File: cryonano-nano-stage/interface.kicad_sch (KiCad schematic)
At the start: 0 parts

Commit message: sch improved
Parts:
- added C29, C32, C33, C34: 1u, Capacitor_SMD:C_0603_1608Metric, symbol Device:C_Small
- added C67: 100n, Capacitor_SMD:C_0603_1608Metric, symbol Device:C_Small
- added C68: 10u, Capacitor_SMD:C_0805_2012Metric, symbol Device:C_Small
- added R41, R42, R43, R44, R51, R53, R55, R56: 10k, Resistor_SMD:R_0603_1608Metric, symbol Device:R_Small
- added R45, R46, R47, R48, R49, R50, R52, R54: 0R, Resistor_SMD:R_0603_1608Metric, symbol Device:R_Small
- added U7, U8: LP5907MFX-3.3_NOPB, SOT95P280X145-5N, symbol symbols:LP5907MFX-3.3_NOPB
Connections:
- new net: R55.2, R56.1
- new net: R49.2, R51.1, R53.2, R55.1
- new net: R41.1, R45.2
- new net: R41.2, R42.1, R44.1, R48.2
- new net: R52.2, R53.1
- new net: R43.1, R44.2
- new net +3V3_1: C32.1, R45.1, U7.5 (OUT)
- new net +3V3_2: C34.1, R52.1, U8.5 (OUT)
- new net +5V0IN: C29.1, C33.1, C67.1, C68.1, U7.1 (IN), U7.3 (EN), U8.1 (IN), U8.3 (EN)
- new net 0V0IN: C29.2, C32.2, C33.2, C34.2, C67.2, C68.2, R46.2, R54.2, U7.2 (GND), U8.2 (GND)
- new net RTD1_A: R42.2
- new net RTD1_B: R43.2, R46.1, R47.2
- new net RTD1_REF+: R48.1
- new net RTD1_REF-: R47.1
- new net RTD2_A: R51.2
- new net RTD2_B: R50.2, R54.1, R56.2
- new net RTD2_REF+: R49.1
- new net RTD2_REF-: R50.1
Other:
- note added: "Power conditioning."
- company: (none) -> Cryonano Labs Pvt. Ltd.
- title: (none) -> Nano stage controller

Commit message: sch improved
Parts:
- C67: now not fitted
- C68: value 10u -> 100n; footprint Capacitor_SMD:C_0805_2012Metric -> Capacitor_SMD:C_0603_1608Metric; Tolerence (none) -> 10%; now not fitted
- R41, R42, R43, R44, R45, R46, R47, R48, R49, R50, R51, R52, R53, R54, R55, R56: footprint Resistor_SMD:R_0603_1608Metric -> Resistor_SMD:R_0805_2012Metric
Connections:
- net EQ2-: now reaches R55.2, R56.1
- net EQ1-: now reaches R43.1, R44.2
- net RTD1_A renamed EQ1+
- net RTD2_A renamed EQ2+

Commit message: sch improved
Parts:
- removed C29, C32, C33, C34: 1u, Capacitor_SMD:C_0603_1608Metric, symbol Device:C_Small
- removed C67, C68: 100n, Capacitor_SMD:C_0603_1608Metric, symbol Device:C_Small
- removed U7, U8: LP5907MFX-3.3_NOPB, SOT95P280X145-5N, symbol symbols:LP5907MFX-3.3_NOPB
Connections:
- net +3V3_2 is gone; now on net EXCITATION: R52.1
- net +3V3_1 renamed EXCITATION
- net 0V0IN renamed REF0
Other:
- note removed: "Power conditioning."
- moved on the sheet: R41, R42, R43, R44, R45, R46, R47, R48, R49, R50, R51, R52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

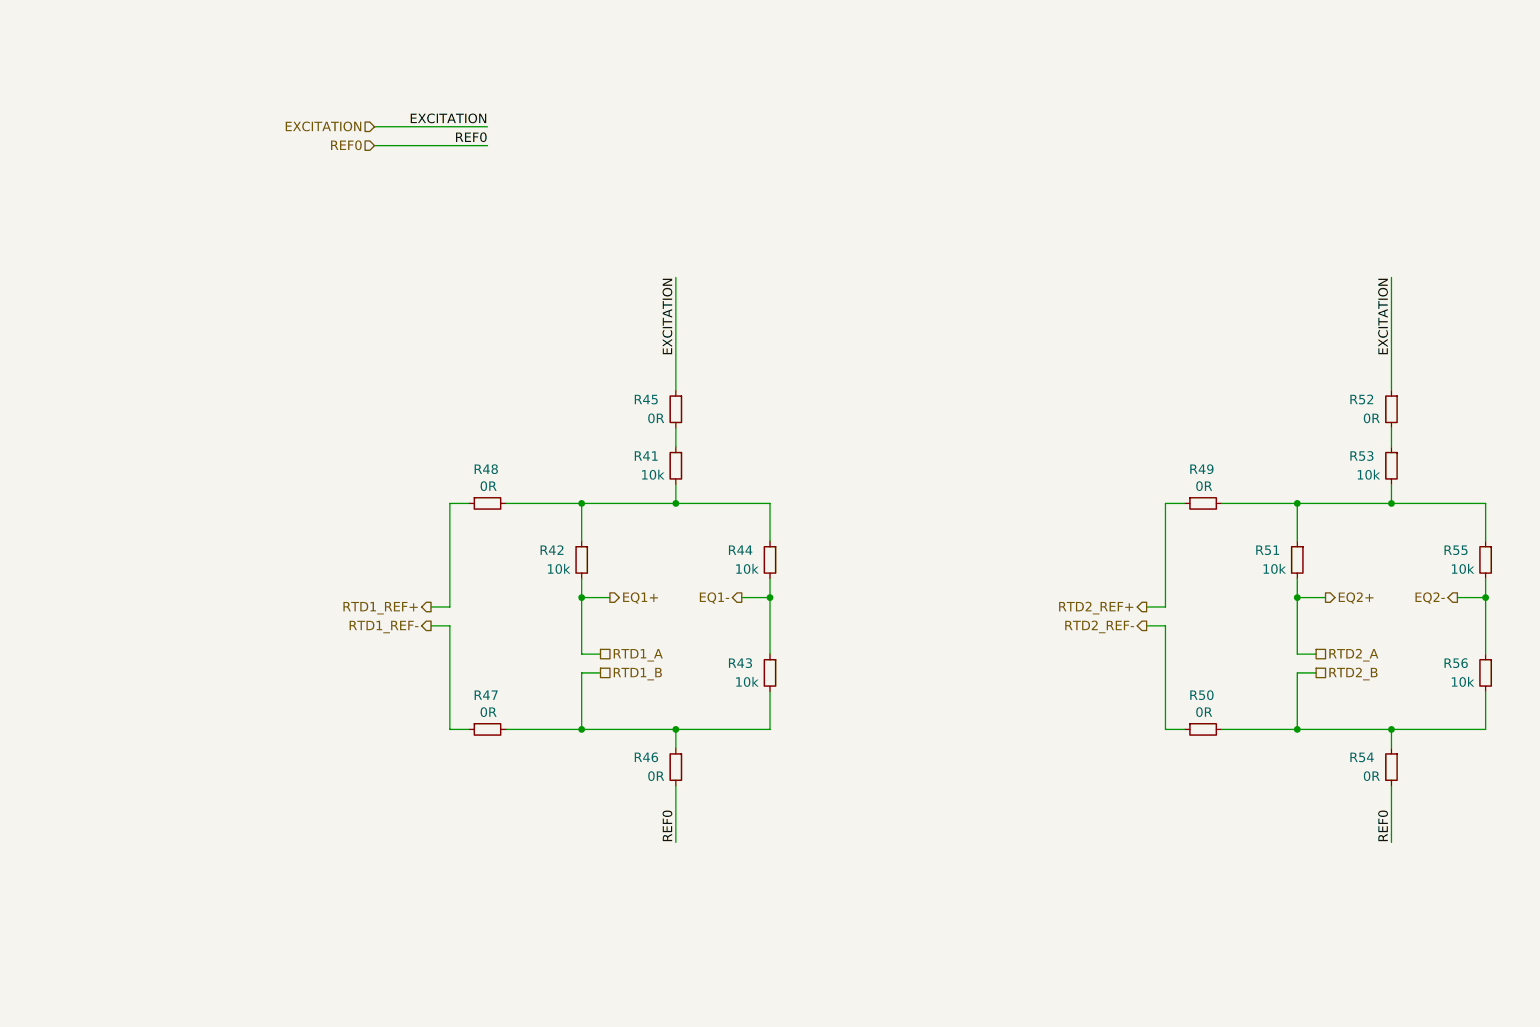
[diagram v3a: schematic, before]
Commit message: pcb drc ok. 68 ohm matching pending
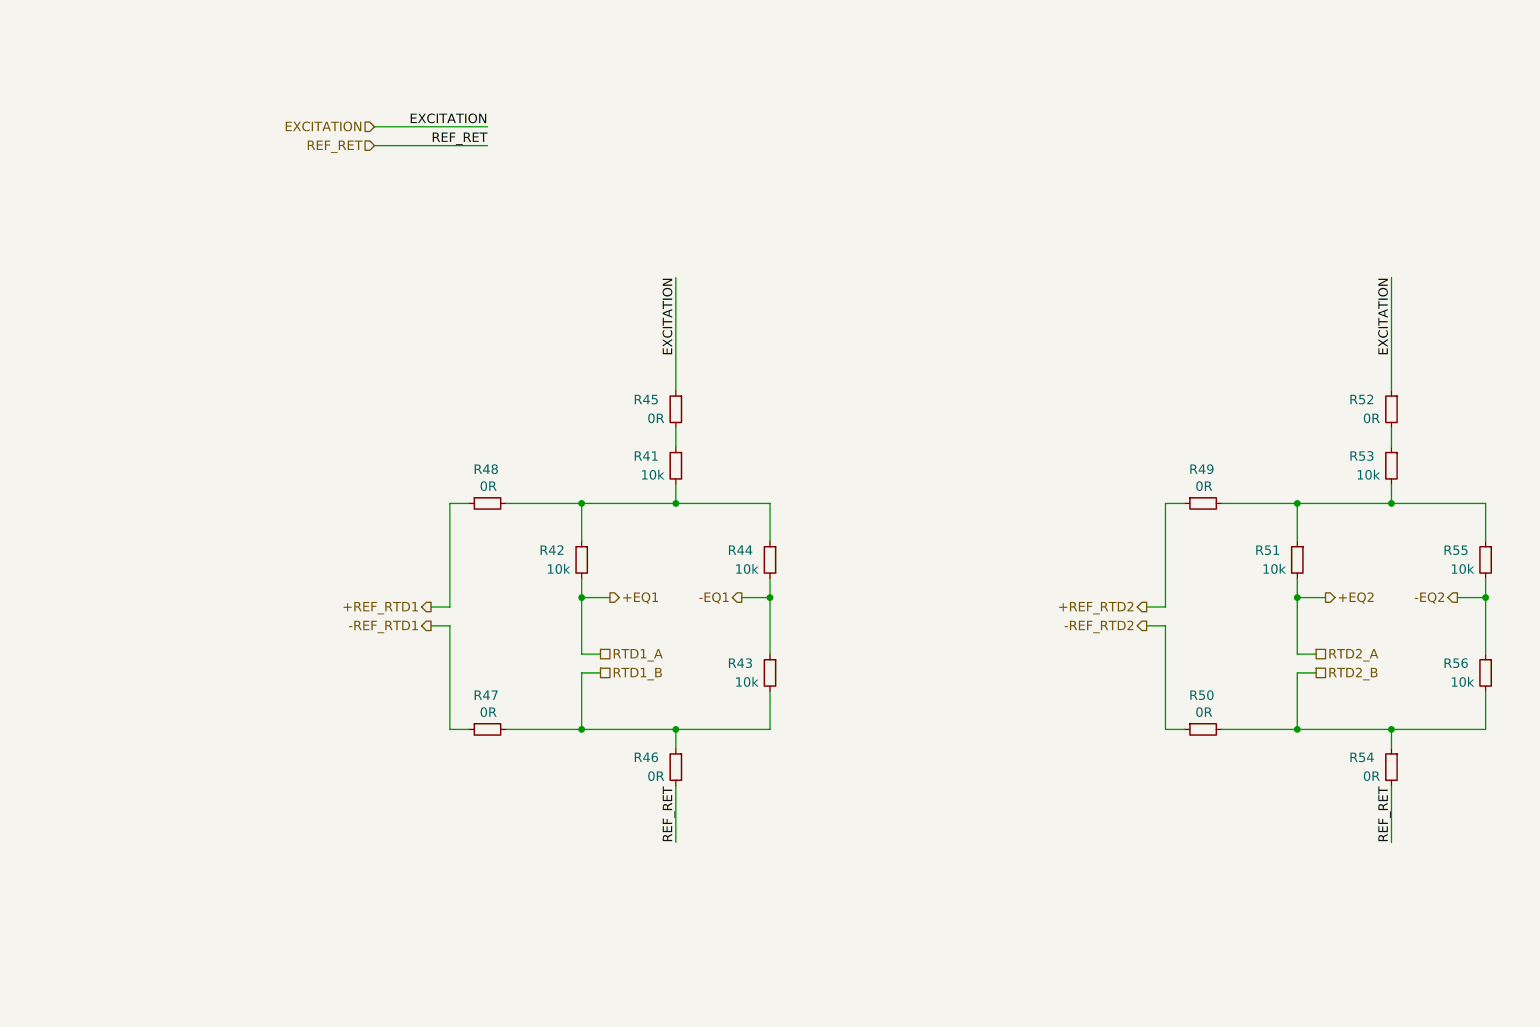
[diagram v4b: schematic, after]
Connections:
- net EQ1+ renamed +EQ1
- net EQ1- renamed -EQ1
- net EQ2+ renamed +EQ2
- net EQ2- renamed -EQ2
- net REF0 renamed REF_RET
- net RTD1_REF+ renamed +REF_RTD1
- net RTD1_REF- renamed -REF_RTD1
- net RTD2_REF+ renamed +REF_RTD2
- net RTD2_REF- renamed -REF_RTD2

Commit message: drc no error, only warnings
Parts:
- R41, R42, R43, R44, R45, R46, R47, R48, R49, R50, R51, R52, R53, R54, R55, R56: footprint Resistor_SMD:R_0805_2012Metric -> Resistor_SMD:R_0805_2012Metric_Pad1.20x1.40mm_HandSolder
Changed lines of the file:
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@@
 			)
 		)
-		(property "Footprint" "Resistor_SMD:R_0805_2012Metric"
+		(property "Footprint" "Resistor_SMD:R_0805_2012Metric_Pad1.20x1.40mm_HandSolder"
 			(at 101.6 124.46 0)
 			(hide yes)
@@
 			)
 		)
-		(property "Footprint" "Resistor_SMD:R_0805_2012Metric"
+		(property "Footprint" "Resistor_SMD:R_0805_2012Metric_Pad1.20x1.40mm_HandSolder"
 			(at 210.82 111.76 0)
 			(hide yes)
@@
 			)
 		)
-		(property "Footprint" "Resistor_SMD:R_0805_2012Metric"
+		(property "Footprint" "Resistor_SMD:R_0805_2012Metric_Pad1.20x1.40mm_HandSolder"
 			(at 172.72 88.9 0)
 			(hide yes)
@@
 			)
 		)
-		(property "Footprint" "Resistor_SMD:R_0805_2012Metric"
+		(property "Footprint" "Resistor_SMD:R_0805_2012Metric_Pad1.20x1.40mm_HandSolder"
 			(at 101.6 83.82 0)
 			(hide yes)
@@
 			)
 		)
-		(property "Footprint" "Resistor_SMD:R_0805_2012Metric"
+		(property "Footprint" "Resistor_SMD:R_0805_2012Metric_Pad1.20x1.40mm_HandSolder"
 			(at 210.82 96.52 0)
 			(hide yes)
@@
 			)
 		)
-		(property "Footprint" "Resistor_SMD:R_0805_2012Metric"
+		(property "Footprint" "Resistor_SMD:R_0805_2012Metric_Pad1.20x1.40mm_HandSolder"
 			(at 101.6 76.2 0)
 			(hide yes)
@@
 			)
 		)
-		(property "Footprint" "Resistor_SMD:R_0805_2012Metric"
+		(property "Footprint" "Resistor_SMD:R_0805_2012Metric_Pad1.20x1.40mm_HandSolder"
 			(at 198.12 83.82 0)
 			(hide yes)
@@
 			)
 		)
-		(property "Footprint" "Resistor_SMD:R_0805_2012Metric"
+		(property "Footprint" "Resistor_SMD:R_0805_2012Metric_Pad1.20x1.40mm_HandSolder"
 			(at 198.12 76.2 0)
 			(hide yes)
@@
 			)
 		)
-		(property "Footprint" "Resistor_SMD:R_0805_2012Metric"
+		(property "Footprint" "Resistor_SMD:R_0805_2012Metric_Pad1.20x1.40mm_HandSolder"
 			(at 172.72 119.38 0)
 			(hide yes)
@@
 			)
 		)
-		(property "Footprint" "Resistor_SMD:R_0805_2012Metric"
+		(property "Footprint" "Resistor_SMD:R_0805_2012Metric_Pad1.20x1.40mm_HandSolder"
 			(at 88.9 96.52 0)
 			(hide yes)
@@
 			)
 		)
-		(property "Footprint" "Resistor_SMD:R_0805_2012Metric"
+		(property "Footprint" "Resistor_SMD:R_0805_2012Metric_Pad1.20x1.40mm_HandSolder"
 			(at 76.2 88.9 0)
 			(hide yes)
@@
 			)
 		)
-		(property "Footprint" "Resistor_SMD:R_0805_2012Metric"
+		(property "Footprint" "Resistor_SMD:R_0805_2012Metric_Pad1.20x1.40mm_HandSolder"
 			(at 76.2 119.38 0)
 			(hide yes)
@@
 			)
 		)
-		(property "Footprint" "Resistor_SMD:R_0805_2012Metric"
+		(property "Footprint" "Resistor_SMD:R_0805_2012Metric_Pad1.20x1.40mm_HandSolder"
 			(at 198.12 124.46 0)
 			(hide yes)
@@
 			)
 		)
-		(property "Footprint" "Resistor_SMD:R_0805_2012Metric"
+		(property "Footprint" "Resistor_SMD:R_0805_2012Metric_Pad1.20x1.40mm_HandSolder"
 			(at 185.42 96.52 0)
 			(hide yes)
@@
 			)
 		)
-		(property "Footprint" "Resistor_SMD:R_0805_2012Metric"
+		(property "Footprint" "Resistor_SMD:R_0805_2012Metric_Pad1.20x1.40mm_HandSolder"
 			(at 114.3 111.76 0)
 			(hide yes)
@@
 			)
 		)
-		(property "Footprint" "Resistor_SMD:R_0805_2012Metric"
+		(property "Footprint" "Resistor_SMD:R_0805_2012Metric_Pad1.20x1.40mm_HandSolder"
 			(at 114.3 96.52 0)
 			(hide yes)

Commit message: bom adjusted
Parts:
- R41, R42, R43, R44, R45, R46, R47, R48, R49, R50, R51, R52, R53, R54, R55, R56: Order No. (none) -> 0805/250mW
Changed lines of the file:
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@@
 			)
 		)
-		(property "Order No." ""
+		(property "Order No." "0805/250mW"
 			(at 101.6 124.46 0)
 			(hide yes)
@@
 			)
 		)
-		(property "Order No." ""
+		(property "Order No." "0805/250mW"
 			(at 210.82 111.76 0)
 			(hide yes)
@@
 			)
 		)
-		(property "Order No." ""
+		(property "Order No." "0805/250mW"
 			(at 172.72 88.9 0)
 			(hide yes)
@@
 			)
 		)
-		(property "Order No." ""
+		(property "Order No." "0805/250mW"
 			(at 101.6 83.82 0)
 			(hide yes)
@@
 			)
 		)
-		(property "Order No." ""
+		(property "Order No." "0805/250mW"
 			(at 210.82 96.52 0)
 			(hide yes)
@@
 			)
 		)
-		(property "Order No." ""
+		(property "Order No." "0805/250mW"
 			(at 101.6 76.2 0)
 			(hide yes)
@@
 			)
 		)
-		(property "Order No." ""
+		(property "Order No." "0805/250mW"
 			(at 198.12 83.82 0)
 			(hide yes)
@@
 			)
 		)
-		(property "Order No." ""
+		(property "Order No." "0805/250mW"
 			(at 198.12 76.2 0)
 			(hide yes)
@@
 			)
 		)
-		(property "Order No." ""
+		(property "Order No." "0805/250mW"
 			(at 172.72 119.38 0)
 			(hide yes)
@@
 			)
 		)
-		(property "Order No." ""
+		(property "Order No." "0805/250mW"
 			(at 88.9 96.52 0)
 			(hide yes)
@@
 			)
 		)
-		(property "Order No." ""
+		(property "Order No." "0805/250mW"
 			(at 76.2 88.9 0)
 			(hide yes)
@@
 			)
 		)
-		(property "Order No." ""
+		(property "Order No." "0805/250mW"
 			(at 76.2 119.38 0)
 			(hide yes)
@@
 			)
 		)
-		(property "Order No." ""
+		(property "Order No." "0805/250mW"
 			(at 198.12 124.46 0)
 			(hide yes)
@@
 			)
 		)
-		(property "Order No." ""
+		(property "Order No." "0805/250mW"
 			(at 185.42 96.52 0)
 			(hide yes)
@@
 			)
 		)
-		(property "Order No." ""
+		(property "Order No." "0805/250mW"
 			(at 114.3 111.76 0)
 			(hide yes)
@@
 			)
 		)
-		(property "Order No." ""
+		(property "Order No." "0805/250mW"
 			(at 114.3 96.52 0)
 			(hide yes)

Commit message: release candidate
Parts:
- added R101, R102: 0R, Resistor_SMD:R_0805_2012Metric_Pad1.20x1.40mm_HandSolder, symbol Device:R_Small
- R41, R42, R43, R44, R45, R46, R47, R48, R49, R50, R51, R52, R53, R54, R55, R56: Order No. 0805/250mW -> 0805, 250mW
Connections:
- net +REF_RTD1: now also R101.1
- net +REF_RTD2: now also R102.1
- net at R41.1, R45.2: now also R101.2
- net at R52.2, R53.1: now also R102.2
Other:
- note added: "Note: Bridge excitation current max <= 5 mA"
- moved on the sheet: R45, R52
